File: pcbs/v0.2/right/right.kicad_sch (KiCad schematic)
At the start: 94 parts, among them SW1 RESET, U1 ProMicro, U2 TRRS

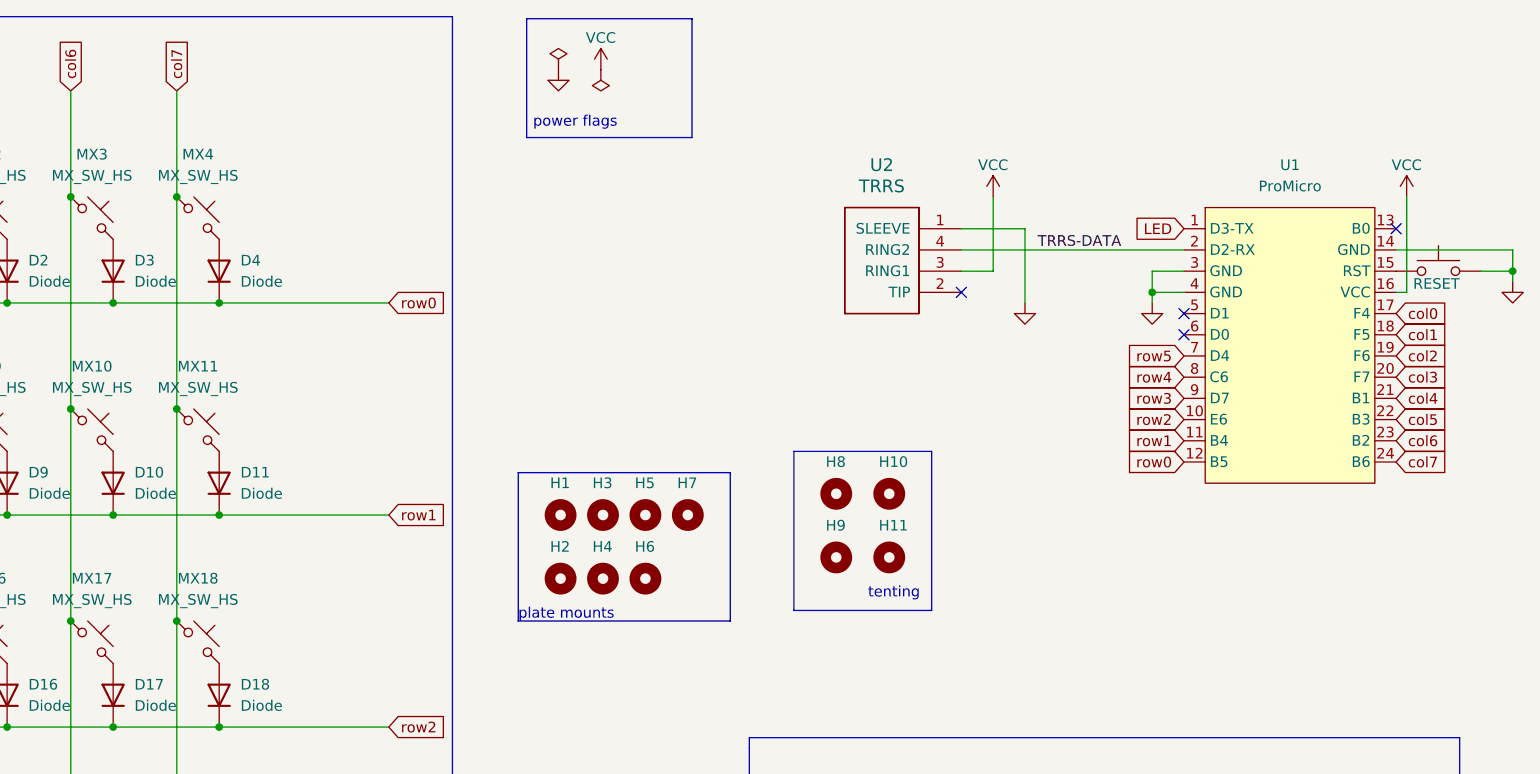
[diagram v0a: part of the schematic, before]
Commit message: Layed out the switches on the PCB
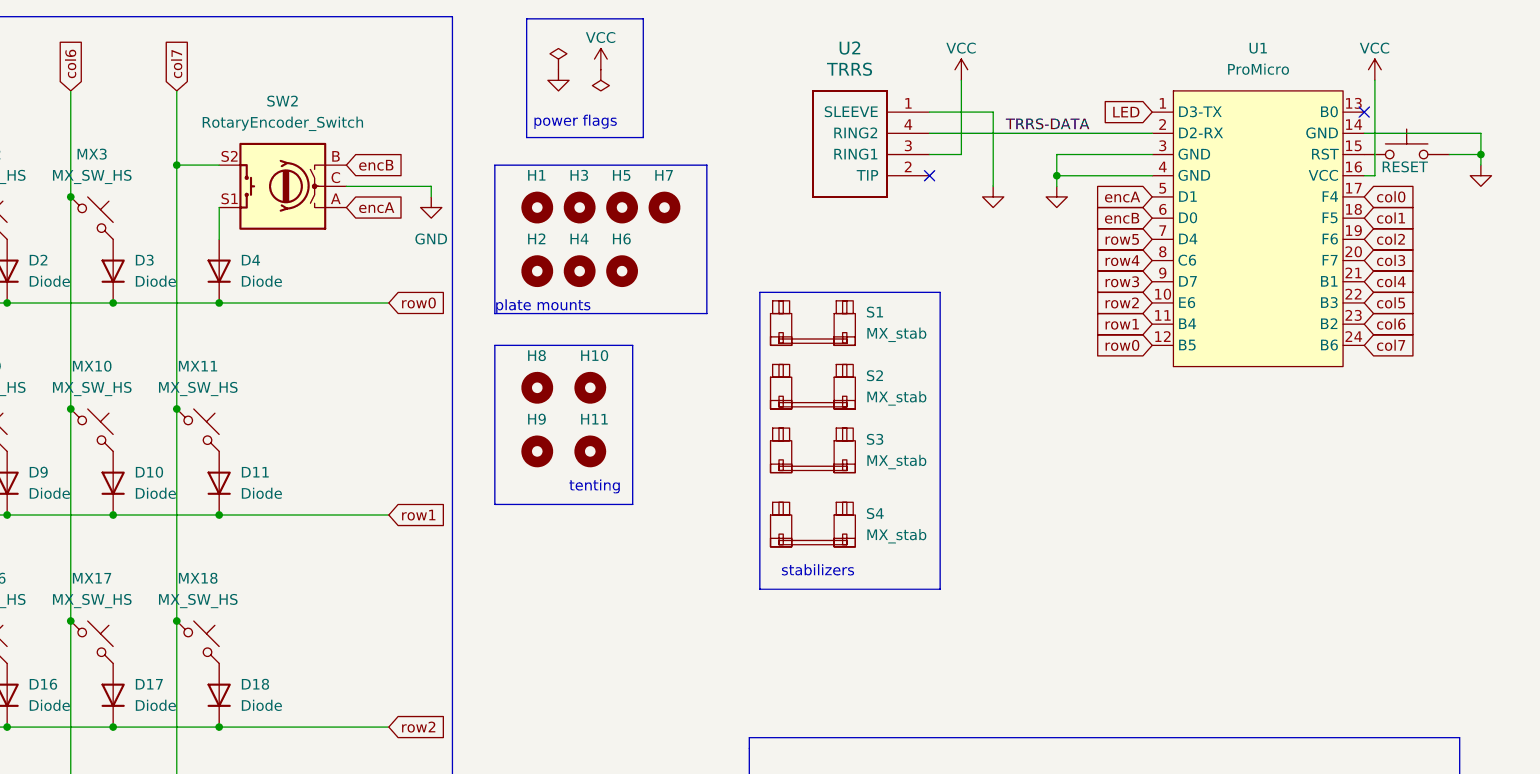
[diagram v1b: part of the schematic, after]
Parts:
- removed MX4: MX_SW_HS, PCM_marbastlib-mx:SW_MX_HS_1u, symbol marbastlib-mx:MX_SW_HS
- added S1, S4: MX_stab, marbastlib-mx:STAB_MX_P_2u, symbol marbastlib-mx:MX_stab
- added S2: MX_stab, marbastlib-mx:STAB_MX_P_2.75u, symbol marbastlib-mx:MX_stab
- added S3: MX_stab, marbastlib-mx:STAB_MX_P_ISO, symbol marbastlib-mx:MX_stab
- added SW2: RotaryEncoder_Switch, Keebio-Parts:RotaryEncoder_EC11, symbol Device:RotaryEncoder_Switch
- MX1, MX10, MX11, MX12, MX13, MX14, MX15, MX16, MX17, MX18, MX19, MX2, MX20, MX21, MX22, MX23, MX24, MX25, MX26, MX27, MX28, MX29, MX3, MX30, MX31, MX32, MX33, MX5, MX6, MX7, MX8, MX9: footprint PCM_marbastlib-mx:SW_MX_HS_1u -> marbastlib-mx:SW_MX_1u
- MX34, MX35, MX36, MX37: footprint PCM_marbastlib-mx:SW_MX_HS_1u -> marbastlib-mx:SW_MX_1.25u
- U1: footprint PCM_marbastlib-xp-promicroish:ProMicro_USBup -> marbastlib-xp-promicroish:ProMicro_Reversible_Single
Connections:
- net GND: now also SW2.C
- net col7: now also SW2.S2
- net at D4.2 (A): now also SW2.S1
- net encA: now reaches U1.5 (D1)
- net encA: now also SW2.A
- net encB: now reaches U1.6 (D0)
- net encB: now also SW2.B
- no-connect marks 5 -> 3
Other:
- note added: "stabilizers"
- moved on the sheet: H1, H10, H11, H2, H3, H4, H5, H6, H7, H8, H9, U1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

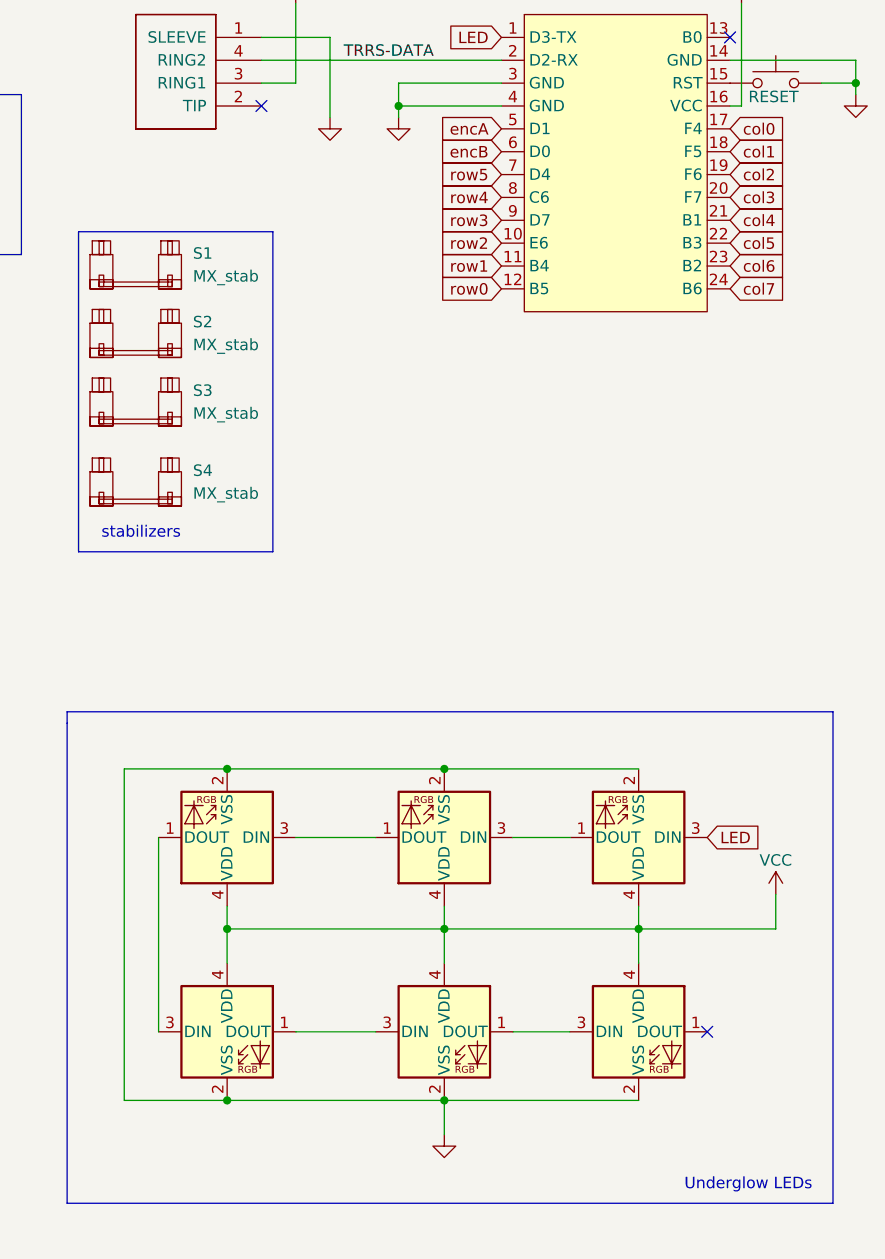
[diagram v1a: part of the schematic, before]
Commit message: Routed PCB traces.
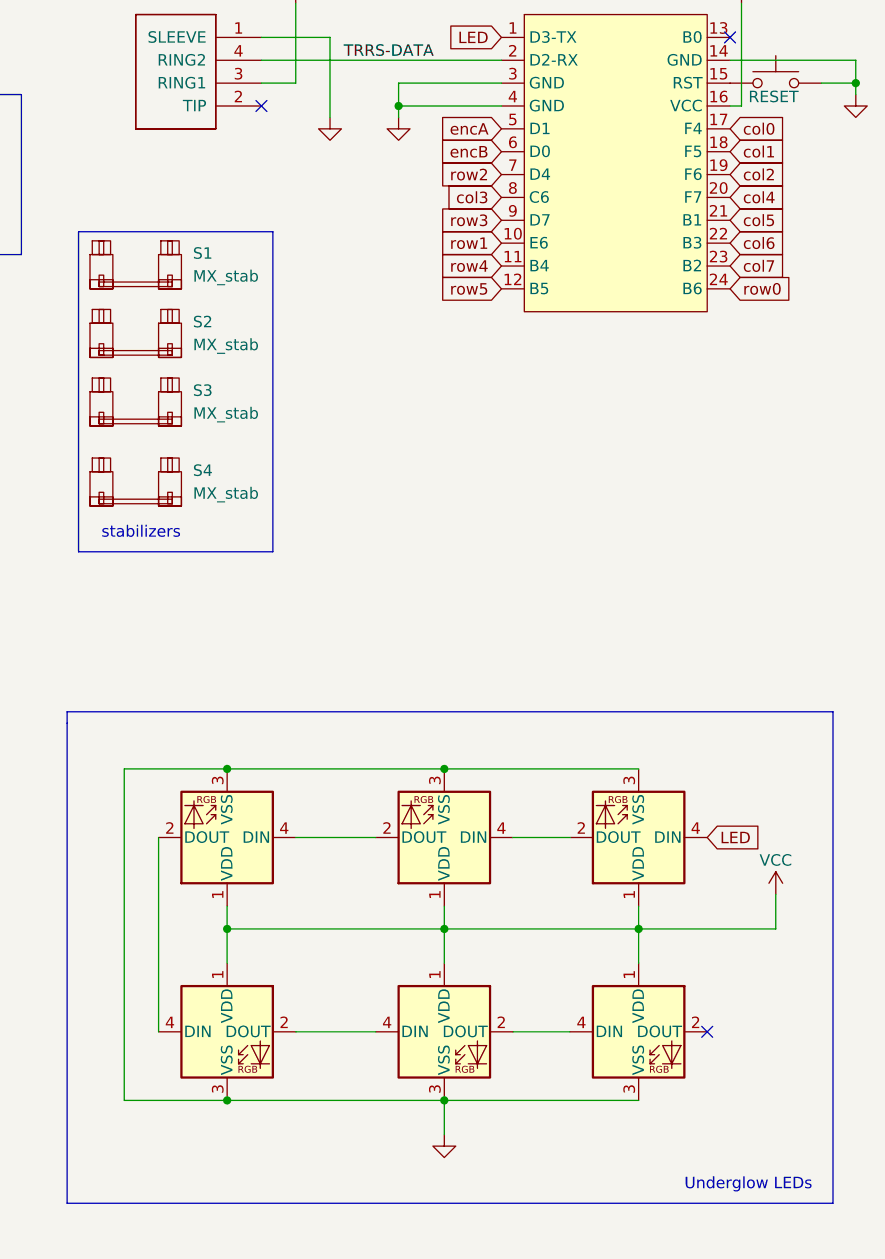
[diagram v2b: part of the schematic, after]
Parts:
- D38, D39, D40, D41, D42, D43: footprint Keebio-Parts:SK6812-MINI-E -> LED_SMD:LED_WS2812B_PLCC4_5.0x5.0mm_P3.2mm; symbol LED:SK6812MINI -> LED:WS2812B
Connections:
- net GND: now also D38.3 (VSS), D39.3 (VSS), D40.3 (VSS), D41.3 (VSS), D42.3 (VSS), D43.3 (VSS); no longer D38.2 (VSS), D39.2 (VSS), D40.2 (VSS), D41.2 (VSS), D42.2 (VSS), D43.2 (VSS)
- net LED: now also D42.4 (DIN); no longer D42.3 (DIN)
- net VCC: now also D38.1 (VDD), D39.1 (VDD), D40.1 (VDD), D41.1 (VDD), D42.1 (VDD), D43.1 (VDD); no longer D38.4 (VDD), D39.4 (VDD), D40.4 (VDD), D41.4 (VDD), D42.4 (VDD), D43.4 (VDD)
- net col3: now also U1.8 (C6); no longer U1.20 (F7)
- net col4: now also U1.20 (F7); no longer U1.21 (B1)
- net col5: now also U1.21 (B1); no longer U1.22 (B3)
- net col6: now also U1.22 (B3); no longer U1.23 (B2)
- net col7: now also U1.23 (B2); no longer U1.24 (B6)
- net row0: now also U1.24 (B6); no longer U1.12 (B5)
- net row1: now also U1.10 (E6); no longer U1.11 (B4)
- net row2: now also U1.7 (D4); no longer U1.10 (E6)
- net row4: now also U1.11 (B4); no longer U1.8 (C6)
- net row5: now also U1.12 (B5); no longer U1.7 (D4)
- new net: D39.2 (DOUT), D41.4 (DIN)
- new net: D38.2 (DOUT), D39.4 (DIN)
- new net: D41.2 (DOUT), D43.4 (DIN)
- new net: D38.4 (DIN), D40.2 (DOUT)
- new net: D40.4 (DIN), D42.2 (DOUT)
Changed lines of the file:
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@@
     )
   )
-  (global_label "col6" (shape input) (at 256.54 53.34 0) (fields_autoplaced)
+  (global_label "col6" (shape input) (at 256.54 50.8 0) (fields_autoplaced)
     (effects (font (size 1.27 1.27)) (justify left))
-    (property "Intersheetrefs" "${INTERSHEET_REFS}" (at 263.6375 53.34 0)
+    (property "Intersheetrefs" "${INTERSHEET_REFS}" (at 263.6375 50.8 0)
       (effects (font (size 1.27 1.27)) (justify left) hide)
     )
@@
     )
   )
-  (global_label "row5" (shape input) (at 231.14 43.18 180) (fields_autoplaced)
+  (global_label "row5" (shape input) (at 231.14 55.88 180) (fields_autoplaced)
     (effects (font (size 1.27 1.27)) (justify right))
-    (property "Intersheetrefs" "${INTERSHEET_REFS}" (at 223.6796 43.18 0)
+    (property "Intersheetrefs" "${INTERSHEET_REFS}" (at 223.6796 55.88 0)
       (effects (font (size 1.27 1.27)) (justify right) hide)
     )
@@
     )
   )
-  (global_label "row4" (shape input) (at 231.14 45.72 180) (fields_autoplaced)
+  (global_label "row4" (shape input) (at 231.14 53.34 180) (fields_autoplaced)
     (effects (font (size 1.27 1.27)) (justify right))
-    (property "Intersheetrefs" "${INTERSHEET_REFS}" (at 223.6796 45.72 0)
+    (property "Intersheetrefs" "${INTERSHEET_REFS}" (at 223.6796 53.34 0)
       (effects (font (size 1.27 1.27)) (justify right) hide)
     )
@@
     )
   )
-  (global_label "row1" (shape input) (at 231.14 53.34 180) (fields_autoplaced)
+  (global_label "row1" (shape input) (at 231.14 50.8 180) (fields_autoplaced)
     (effects (font (size 1.27 1.27)) (justify right))
-    (property "Intersheetrefs" "${INTERSHEET_REFS}" (at 223.6796 53.34 0)
+    (property "Intersheetrefs" "${INTERSHEET_REFS}" (at 223.6796 50.8 0)
       (effects (font (size 1.27 1.27)) (justify right) hide)
     )
   )
-  (global_label "col3" (shape input) (at 256.54 45.72 0) (fields_autoplaced)
-    (effects (font (size 1.27 1.27)) (justify left))
-    (property "Intersheetrefs" "${INTERSHEET_REFS}" (at 263.6375 45.72 0)
-      (effects (font (size 1.27 1.27)) (justify left) hide)
+  (global_label "col3" (shape input) (at 231.14 45.72 180) (fields_autoplaced)
+    (effects (font (size 1.27 1.27)) (justify right))
+    (property "Intersheetrefs" "${INTERSHEET_REFS}" (at 224.0425 45.72 0)
+      (effects (font (size 1.27 1.27)) (justify right) hide)
     )
   )
@@
     )
   )
-  (global_label "col5" (shape input) (at 256.54 50.8 0) (fields_autoplaced)
-    (effects (font (size 1.27 1.27)) (justify left))
-    (property "Intersheetrefs" "${INTERSHEET_REFS}" (at 263.6375 50.8 0)
-      (effects (font (size 1.27 1.27)) (justify left) hide)
-    )
-  )
-  (global_label "col4" (shape input) (at 256.54 48.26 0) (fields_autoplaced)
+  (global_label "col5" (shape input) (at 256.54 48.26 0) (fields_autoplaced)
     (effects (font (size 1.27 1.27)) (justify left))
     (property "Intersheetrefs" "${INTERSHEET_REFS}" (at 263.6375 48.26 0)
+      (effects (font (size 1.27 1.27)) (justify left) hide)
+    )
+  )
+  (global_label "col4" (shape input) (at 256.54 45.72 0) (fields_autoplaced)
+    (effects (font (size 1.27 1.27)) (justify left))
+    (property "Intersheetrefs" "${INTERSHEET_REFS}" (at 263.6375 45.72 0)
       (effects (font (size 1.27 1.27)) (justify left) hide)
     )
@@
     )
   )
-  (global_label "row2" (shape input) (at 231.14 50.8 180) (fields_autoplaced)
+  (global_label "row2" (shape input) (at 231.14 43.18 180) (fields_autoplaced)
     (effects (font (size 1.27 1.27)) (justify right))
-    (property "Intersheetrefs" "${INTERSHEET_REFS}" (at 223.6796 50.8 0)
+    (property "Intersheetrefs" "${INTERSHEET_REFS}" (at 223.6796 43.18 0)
       (effects (font (size 1.27 1.27)) (justify right) hide)
     )
   )
-  (global_label "col7" (shape input) (at 256.54 55.88 0) (fields_autoplaced)
+  (global_label "col7" (shape input) (at 256.54 53.34 0) (fields_autoplaced)
     (effects (font (size 1.27 1.27)) (justify left))
-    (property "Intersheetrefs" "${INTERSHEET_REFS}" (at 263.6375 55.88 0)
-      (effects (font (size 1.27 1.27)) (justify left) hide)
-    )
-  )
-  (global_label "row0" (shape input) (at 231.14 55.88 180) (fields_autoplaced)
-    (effects (font (size 1.27 1.27)) (justify right))
-    (property "Intersheetrefs" "${INTERSHEET_REFS}" (at 223.6796 55.88 0)
-      (effects (font (size 1.27 1.27)) (justify right) hide)
+    (property "Intersheetrefs" "${INTERSHEET_REFS}" (at 263.6375 53.34 0)
+      (effects (font (size 1.27 1.27)) (justify left) hide)
+    )
+  )
+  (global_label "row0" (shape input) (at 256.54 55.88 0) (fields_autoplaced)
+    (effects (font (size 1.27 1.27)) (justify left))
+    (property "Intersheetrefs" "${INTERSHEET_REFS}" (at 264.0004 55.88 0)
+      (effects (font (size 1.27 1.27)) (justify left) hide)
     )
   )
@@
     )
   )
-  (symbol (lib_id "LED:SK6812MINI") (at 200.66 138.43 0) (unit 1)
+  (symbol (lib_id "LED:WS2812B") (at 200.66 138.43 0) (unit 1)
     (in_bom yes) (on_board yes) (dnp no) (fields_autoplaced)
     (property "Reference" "D39" (at 213.36 134.7821 0)
@@
       (effects (font (size 1.27 1.27)) hide)
     )
-    (property "Footprint" "Keebio-Parts:SK6812-MINI-E" (at 201.93 146.05 0)
+    (property "Footprint" "LED_SMD:LED_WS2812B_PLCC4_5.0x5.0mm_P3.2mm" (at 201.93 146.05 0)
       (effects (font (size 1.27 1.27)) (justify left top) hide)
     )
-    (property "Datasheet" "https://cdn-shop.adafruit.com/product-files/2686/SK6812MINI_REV.01-1-2.pdf" (at 203.2 147.955 0)
+    (property "Datasheet" "https://cdn-shop.adafruit.com/datasheets/WS2812B.pdf" (at 203.2 147.955 0)
       (effects (font (size 1.27 1.27)) (justify left top) hide)
     )
@@
     )
   )
-  (symbol (lib_id "LED:SK6812MINI") (at 246.38 138.43 0) (unit 1)
+  (symbol (lib_id "LED:WS2812B") (at 246.38 138.43 0) (unit 1)
     (in_bom yes) (on_board yes) (dnp no) (fields_autoplaced)
     (property "Reference" "D43" (at 259.08 134.7821 0)
@@
       (effects (font (size 1.27 1.27)) hide)
     )
-    (property "Footprint" "Keebio-Parts:SK6812-MINI-E" (at 247.65 146.05 0)
+    (property "Footprint" "LED_SMD:LED_WS2812B_PLCC4_5.0x5.0mm_P3.2mm" (at 247.65 146.05 0)
       (effects (font (size 1.27 1.27)) (justify left top) hide)
     )
-    (property "Datasheet" "https://cdn-shop.adafruit.com/product-files/2686/SK6812MINI_REV.01-1-2.pdf" (at 248.92 147.955 0)
+    (property "Datasheet" "https://cdn-shop.adafruit.com/datasheets/WS2812B.pdf" (at 248.92 147.955 0)
       (effects (font (size 1.27 1.27)) (justify left top) hide)
     )
@@
     )
   )
-  (symbol (lib_id "LED:SK6812MINI") (at 200.66 116.84 180) (unit 1)
+  (symbol (lib_id "LED:WS2812B") (at 200.66 116.84 180) (unit 1)
     (in_bom yes) (on_board yes) (dnp no) (fields_autoplaced)
     (property "Reference" "D38" (at 187.96 120.4879 0)
@@
       (effects (font (size 1.27 1.27)) hide)
     )
-    (property "Footprint" "Keebio-Parts:SK6812-MINI-E" (at 199.39 109.22 0)
+    (property "Footprint" "LED_SMD:LED_WS2812B_PLCC4_5.0x5.0mm_P3.2mm" (at 199.39 109.22 0)
       (effects (font (size 1.27 1.27)) (justify left top) hide)
     )
-    (property "Datasheet" "https://cdn-shop.adafruit.com/product-files/2686/SK6812MINI_REV.01-1-2.pdf" (at 198.12 107.315 0)
+    (property "Datasheet" "https://cdn-shop.adafruit.com/datasheets/WS2812B.pdf" (at 198.12 107.315 0)
       (effects (font (size 1.27 1.27)) (justify left top) hide)
     )
@@
     )
   )
-  (symbol (lib_id "LED:SK6812MINI") (at 246.38 116.84 180) (unit 1)
+  (symbol (lib_id "LED:WS2812B") (at 246.38 116.84 180) (unit 1)
     (in_bom yes) (on_board yes) (dnp no) (fields_autoplaced)
     (property "Reference" "D42" (at 233.68 120.4879 0)
@@
       (effects (font (size 1.27 1.27)) hide)
     )
-    (property "Footprint" "Keebio-Parts:SK6812-MINI-E" (at 245.11 109.22 0)
+    (property "Footprint" "LED_SMD:LED_WS2812B_PLCC4_5.0x5.0mm_P3.2mm" (at 245.11 109.22 0)
       (effects (font (size 1.27 1.27)) (justify left top) hide)
     )
-    (property "Datasheet" "https://cdn-shop.adafruit.com/product-files/2686/SK6812MINI_REV.01-1-2.pdf" (at 243.84 107.315 0)
+    (property "Datasheet" "https://cdn-shop.adafruit.com/datasheets/WS2812B.pdf" (at 243.84 107.315 0)
       (effects (font (size 1.27 1.27)) (justify left top) hide)
     )
@@
     )
   )
-  (symbol (lib_id "LED:SK6812MINI") (at 224.79 116.84 180) (unit 1)
+  (symbol (lib_id "LED:WS2812B") (at 224.79 116.84 180) (unit 1)
     (in_bom yes) (on_board yes) (dnp no) (fields_autoplaced)
     (property "Reference" "D40" (at 212.09 120.4879 0)
@@
       (effects (font (size 1.27 1.27)) hide)
     )
-    (property "Footprint" "Keebio-Parts:SK6812-MINI-E" (at 223.52 109.22 0)
+    (property "Footprint" "LED_SMD:LED_WS2812B_PLCC4_5.0x5.0mm_P3.2mm" (at 223.52 109.22 0)
       (effects (font (size 1.27 1.27)) (justify left top) hide)
     )
-    (property "Datasheet" "https://cdn-shop.adafruit.com/product-files/2686/SK6812MINI_REV.01-1-2.pdf" (at 222.25 107.315 0)
+    (property "Datasheet" "https://cdn-shop.adafruit.com/datasheets/WS2812B.pdf" (at 222.25 107.315 0)
       (effects (font (size 1.27 1.27)) (justify left top) hide)
     )
@@
     )
   )
-  (symbol (lib_id "LED:SK6812MINI") (at 224.79 138.43 0) (unit 1)
+  (symbol (lib_id "LED:WS2812B") (at 224.79 138.43 0) (unit 1)
     (in_bom yes) (on_board yes) (dnp no) (fields_autoplaced)
     (property "Reference" "D41" (at 237.49 134.7821 0)
@@
       (effects (font (size 1.27 1.27)) hide)
     )
-    (property "Footprint" "Keebio-Parts:SK6812-MINI-E" (at 226.06 146.05 0)
+    (property "Footprint" "LED_SMD:LED_WS2812B_PLCC4_5.0x5.0mm_P3.2mm" (at 226.06 146.05 0)
       (effects (font (size 1.27 1.27)) (justify left top) hide)
     )
-    (property "Datasheet" "https://cdn-shop.adafruit.com/product-files/2686/SK6812MINI_REV.01-1-2.pdf" (at 227.33 147.955 0)
+    (property "Datasheet" "https://cdn-shop.adafruit.com/datasheets/WS2812B.pdf" (at 227.33 147.955 0)
       (effects (font (size 1.27 1.27)) (justify left top) hide)
     )
